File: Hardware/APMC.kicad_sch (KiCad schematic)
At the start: 157 parts, among them J1 Pin header Male 2x7 P:1.27, J10 Conn_01x03, J11 Conn_01x03, J12 Conn_02x08, J13 Conn_01x03, J14 Conn_01x04, J2 USB-C receptacle, J5 Terminal 1x5 P:3.5mm, J6 Terminal 1x5 P:3.5mm, J7 Terminal 1x5 P:3.5mm, J8 Conn_01x04, J9 Conn_01x04, M1 Logo_Open_Hardware_Small, Q1 DMP6023LE, Q2 DMP6023LE, Q3 DMP6023LE, Q4 BSS123, Q5 DMP6023LE, Q6 DMP6023LE, Q7 BSS123, Q8 DMP3056L, U1 LMR51610, U10 TXU0202, U11 PCA9306, U12 LM74703/LM74704, U13 TPS62162DSG, U2 LCFE201202A, U3 TXU0202, U4 M95P32, U5 STM32U575CITx, U6 XTR200, U7 TPS7A2031PDBVR, U8 XTR200, U9 ADS1x2S14, X1 SiT8008Bx-7x, Y1 32.768kHz

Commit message: post-prod fixes
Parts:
- C28: value 1uF/4V -> 4.7uF/4V; footprint Capacitor_SMD:C_0603_1608Metric_Pad1.08x0.95mm_HandSolder -> Custom:C_0603_1608Metric_Pad0.98x0.95mm_HandSolder; Mfg TDK: CGA3E2X5R1A105K080AA -> Samasung: CL10B475KQ8NQNC; Mouser 810-CGA3E2X5R1A105KA -> 187-CL10B475KQ8NQNC; Remarks (none) -> ESR < 20 mΩ @ 3 MHz
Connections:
- net GND: now also C28.1; no longer C28.2
- net VDDA: now also C28.2; no longer C28.1

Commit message: initial firmware
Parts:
- J1: footprint Custom:PinHeader_2x07_P1.27mm_Horizontal -> Custom:PinHeader_2x07_P1.27mm_Horizontal-UP
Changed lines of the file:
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@@
 			)
 		)
-		(property "Footprint" "Custom:PinHeader_2x07_P1.27mm_Horizontal"
+		(property "Footprint" "Custom:PinHeader_2x07_P1.27mm_Horizontal-UP"
 			(at 241.3 26.67 0)
 			(hide yes)

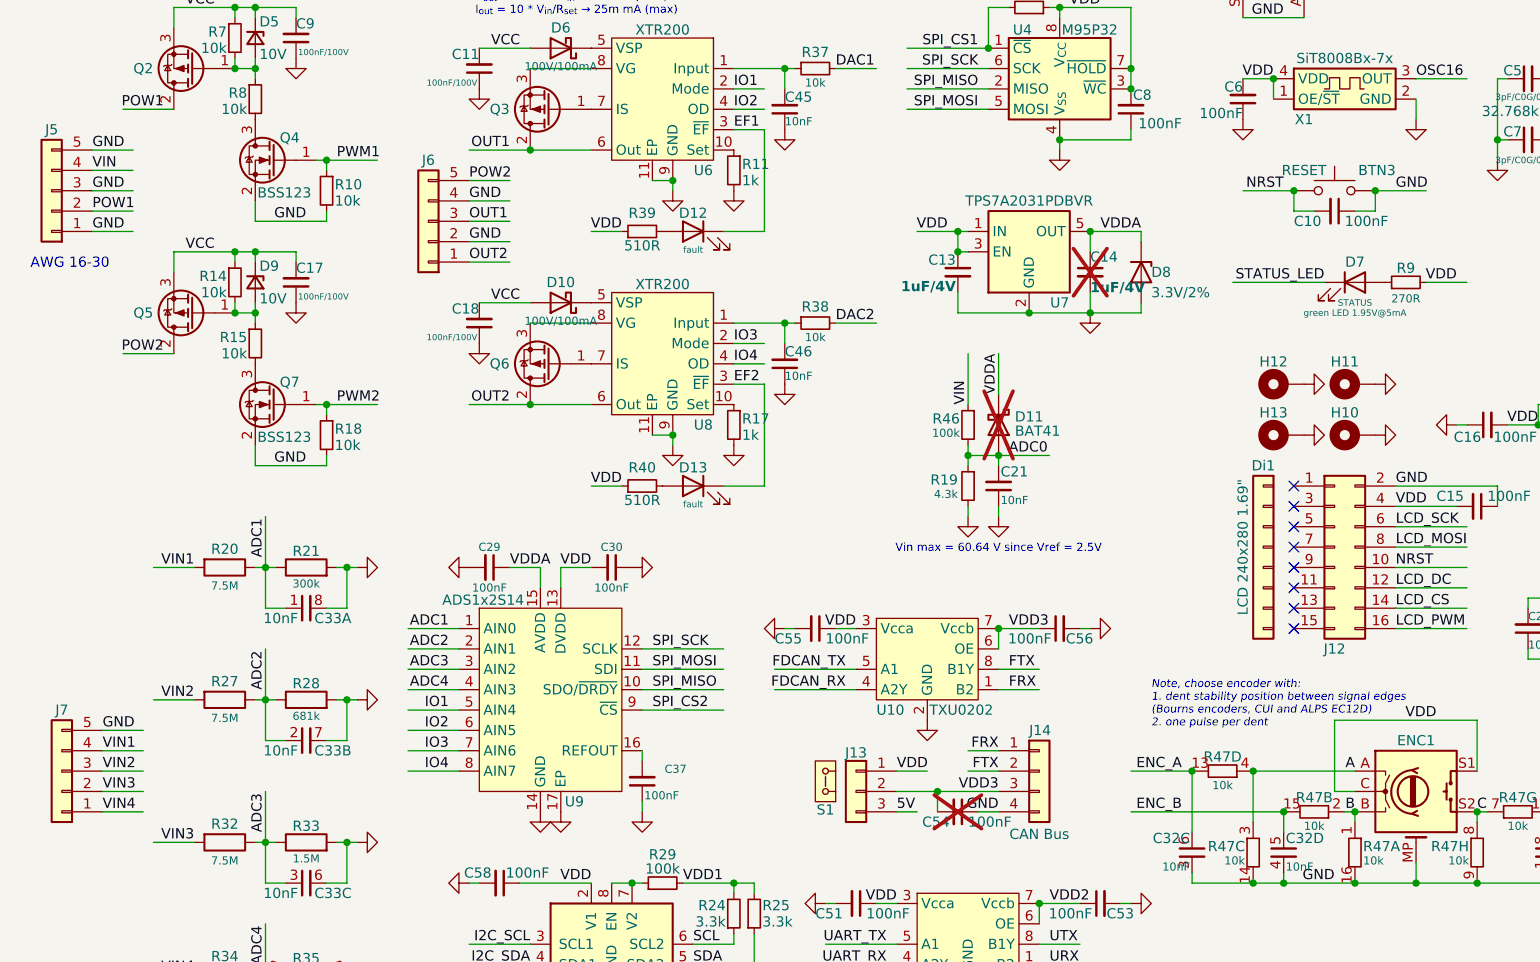
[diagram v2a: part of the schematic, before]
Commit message: LCD pin header modified
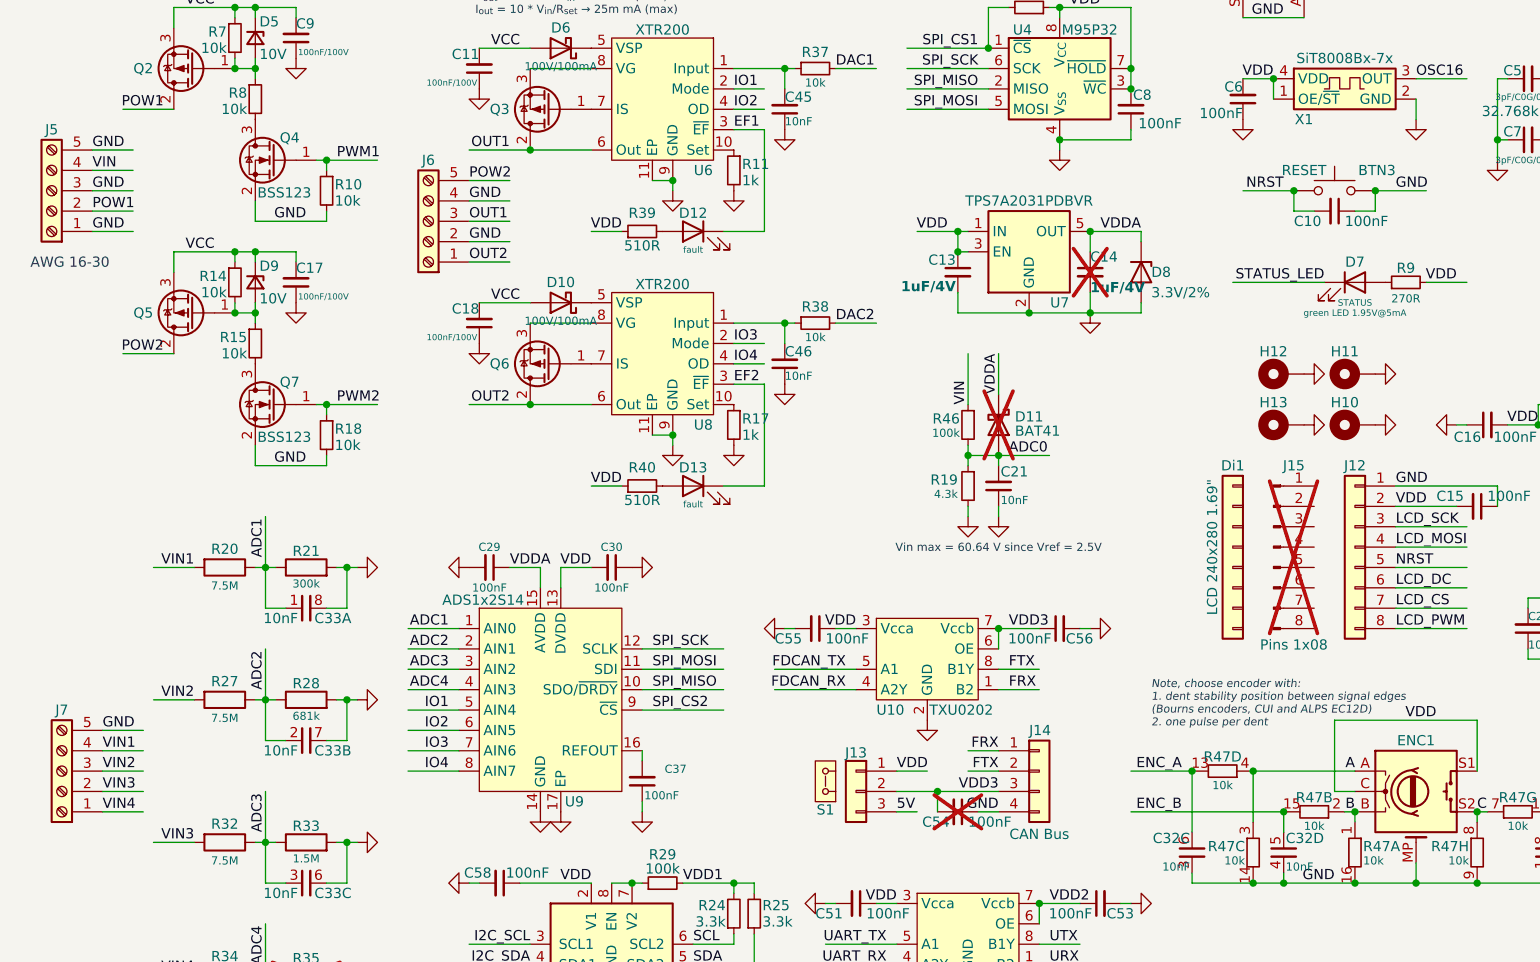
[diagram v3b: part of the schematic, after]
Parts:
- added J15: Pins 1x08, symbol Connector:Conn_01x08_Pin
- J12: value Conn_02x08 -> Conn_01x08; footprint Custom:Harwin_M20-7810845_2x08_P2.54mm_Vertical -> Custom:PinHeader_1x08_P2.54mm_Vertical; symbol Connector_Generic:Conn_02x08_Odd_Even -> Connector_Generic:Conn_01x08; Alt Harwin: M20-7810845, M20-7810845R (2x8, 3.55mm), GCT: BG125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 -> 3M: 929870-01-08-RA, 929984-01-08-RK (H: 3.8mm), Samtec: SL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; Mfg Harwin: M20-7810845 -> 3M: 929870-01-08-30; Mouser 855-M20-7810845 -> 517-929870-01-08-30
- J5, J6, J7: symbol Connector_Generic:Conn_01x05 -> Connector:Screw_Terminal_01x05
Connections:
- net GND: now also J12.1 (Pin_1); no longer J12.2 (Pin_2)
- net LCD_CS: now also J12.7 (Pin_7); no longer J12.14 (Pin_14)
- net LCD_DC: now also J12.6 (Pin_6); no longer J12.12 (Pin_12)
- net LCD_MOSI: now also J12.4 (Pin_4); no longer J12.8 (Pin_8)
- net LCD_PWM: now also J12.8 (Pin_8); no longer J12.16 (Pin_16)
- net LCD_SCK: now also J12.3 (Pin_3); no longer J12.6 (Pin_6)
- net NRST: now also J12.5 (Pin_5); no longer J12.10 (Pin_10)
- net VDD: now also J12.2 (Pin_2); no longer J12.4 (Pin_4)
- no-connect marks 18 -> 10
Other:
- moved on the sheet: Di1, H10, H11, H12, H13

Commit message: rev 2.1 work in progress
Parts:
- removed BTN2: tactile switch 6x6, Custom:tactile_switch_6x6, symbol Switch:SW_Push
- removed C33: 10nF, Custom:RC_Array_Isolated_4_0805, symbol RC_Arrays:C_Array_04_Isolated
- removed Q8: DMP3056L, Package_TO_SOT_SMD:SOT-23, symbol Transistor_FET:VP0610T
- removed R37, R38: 10k, Resistor_SMD:R_0603_1608Metric_Pad0.98x0.95mm_HandSolder, symbol Device:R_Small
- removed R42: 19.1k, Resistor_SMD:R_0603_1608Metric_Pad0.98x0.95mm_HandSolder, symbol Device:R_Small
- removed R43: 100k, Resistor_SMD:R_0603_1608Metric_Pad0.98x0.95mm_HandSolder, symbol Device:R_Small
- removed U1: LMR51610, Package_TO_SOT_SMD:SOT-23-6, symbol LMR51610:LMR51610
- added BTN3: tactile switch 6x6, tactile_switch_6x6_LED, symbol Switch:SW_Push_LED
- added BTN4: SW_Push, Custom:Schurter_MCS-18a, symbol Switch:SW_Push
- added C1, C38, C43: 1uF/10V, Custom:C_0603_1608Metric_Pad0.98x0.95mm_HandSolder, symbol Device:C_Small
- added C31, C33: 1.5nF, Custom:C_0603_1608Metric_Pad0.98x0.95mm_HandSolder, symbol Device:C_Small
- added C34: 100nF, Custom:C_0603_1608Metric_Pad0.98x0.95mm_HandSolder, symbol Device:C_Small
- added C52, C57, C59, C60: 100pF, Custom:0603_0805, symbol Device:C_Small
- added CAP1: M2.5x7, symbol Mechanical:MountingHole
- added D15: Red LED, Custom:LED_0603_1608Metric_Pad1.05x0.95mm_HandSolder, symbol Device:LED
- added D16: TVS 5V U, Custom:D_SOD-123F, symbol Device:D_Zener
- added D57: SS10200HE, Custom:D_SOD-123F, symbol Device:D_Schottky
- added R16: 100k, Resistor_SMD:R_0603_1608Metric_Pad0.98x0.95mm_HandSolder, symbol Device:R_Small
- added R219: 330R/200mA, Resistor_SMD:R_0603_1608Metric_Pad0.98x0.95mm_HandSolder, symbol Device:FerriteBead_Small
- added R22: 5.6k, Resistor_SMD:R_0603_1608Metric_Pad0.98x0.95mm_HandSolder, symbol Device:R_Small
- added R23: 680R, Resistor_SMD:R_0603_1608Metric_Pad0.98x0.95mm_HandSolder, symbol Device:R_Small
- added R4: 360k, Resistor_SMD:R_0603_1608Metric_Pad0.98x0.95mm_HandSolder, symbol Device:R_Small
- added R48, R51: 162k, Resistor_SMD:R_0603_1608Metric_Pad0.98x0.95mm_HandSolder, symbol Device:R_Small
- added R49, R50: 115k, Resistor_SMD:R_0603_1608Metric_Pad0.98x0.95mm_HandSolder, symbol Device:R_Small
- added R52: 64.9k, Resistor_SMD:R_0603_1608Metric_Pad0.98x0.95mm_HandSolder, symbol Device:R_Small
- added U14: OPA2387DSG, Custom:WSON-8-1EP_2x2mm_P0.5mm_EP0.9x1.6mm, symbol Amplifier_Operational:OPA2333xxDRB
- added U15: TPS259461A, Custom:VQFN-HR-10-RPW, symbol TPS2597:TPS259461
- added U16: TUSB320, Package_DFN_QFN:Texas_X2QFN-12_1.6x1.6mm_P0.4mm, symbol TUSB320:TUSB320
- added U17: LMR38015, Custom:TI_WSON-12-1EP_3x3mm_P0.5mm_EP1.3x2.5mm_ThermalVias, symbol LMR380xx:LMR380xx
- BTN2: renamed from BTN1; Alt PTS125SK12-2 LFS, 95C12B4T, 430162085826, TL1100F160Q4JBLK,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 -> TS26-68-25-G-260-SMT-TR; Alt2 (none) -> PTS125SK12-2 LFS, 95C12B4T, 430162085826, TL1100F160Q4JBLK,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; now left out of the parts list
- C13: value 1uF/4V -> 4.7uF/6.3; footprint Capacitor_SMD:C_0603_1608Metric_Pad1.08x0.95mm_HandSolder -> Custom:C_0603_1608Metric_Pad0.98x0.95mm_HandSolder; Mfg TDK: CGA3E2X5R1A105K080AA -> Samasung: CL10B475KQ8NQNC; Mouser 810-CGA3E2X5R1A105KA -> 187-CL10B475KQ8NQNC; Remarks (none) -> ESR < 20 mΩ @ 3 MHz
- C21, C39: Remarks 5%, low-profile (h ≤ 0.5 mm) -> 10%
- C28: value 4.7uF/4V -> 1uF/10V; Mfg Samasung: CL10B475KQ8NQNC -> TDK: CGA3E2X5R1A105M080AA; Mouser 187-CL10B475KQ8NQNC -> 810-CGA3E2X5R1A105MA; Remarks ESR < 20 mΩ @ 3 MHz -> (none)
- C45, C46: value 10nF -> 100pF; Mfg Murata: GRM1857U1A103JA44D -> Samsung: CL10C101JB8NNNC; Mouser 81-GRM1857U1A103JA4D -> 187-CL10C101JB8NNNC; Remarks 5%, low-profile (h ≤ 0.5 mm) -> 5%
- D10: Alt BAT46WJF, BAT46WSHE3-TP, GSBAT46WS, NSR02100HT1G -> BAT46WS, BAT46WJF, BAT46WSHE3-TP, GSBAT46WS, NSR02100HT1G
- Di1: Remarks (none) -> total thickness: 3 mm
- J12: Alt 3M: 929870-01-08-RA, 929984-01-08-RK (H: 3.8mm), Samtec: SL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 -> 3M: 929870-01-08-RA (H: 3.8mm), 929984-01-08-RK (H: 3.8mm),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; Alt2 expensive spring-loaded connector Mill-Max: 821-22-008-10-002101 -> expensive spring-loaded connector Mill-Max: 821-22-008-10-002101 (H: 3.6 mm)
- J15: Remarks Pins to be used with Samtec SL-108-xx and SX-108-xx round p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 -> Pins to be used with Samtec SL-108-x-E (H: 1.78 mm), SL-108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
- J2: value USB-C receptacle -> USB4105-GF-A; symbol Connector:USB_C_Receptacle_USB2.0_16P -> USB_C_Receptacle:USB_C_Receptacle_USB2.0_14P
- L1: value 33uH -> 22uH
- Q1: value DMP6023LE -> FDT86102LZ; Alt TSMC: TSM950N10CW RPG -> (none)
- Q2, Q3, Q5, Q6: Alt MCC: MCT090P10L-TP -> Toshiba: SSM3K7002CFU,LF, NXP: NX138BKWX, DiodesInc: DMN62D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
- R1: value 5.1k -> 11R; Mfg Susumu: RR0816P-512-D -> Susumu: RR0816Q-110-D; Mouser 754-RR0816P-512D -> 754-RR0816Q-110D
- R11, R17: value 1k -> 1.69k; Mfg Susumu: RG1608P-102-B-T5 -> Yageo: RT0603BRD071K69L; Mouser 754-RG1608P-102-B-T5 -> 603-RT0603BRD071K69L
- R2: value 5.1k -> 887k; Mfg Susumu: RR0816P-512-D -> Yageo: RT0603BRD07887KL; Mouser 754-RR0816P-512D -> 603-RT0603BRD07887KL; Remarks 1% -> 1%, resistance must be between 855k - 920k
- R20, R21, R27, R28, R32, R33, R34, R35: footprint Resistor_SMD:R_0805_2012Metric -> Custom:0603_0805
- R29, R44, R6: Mfg Susumu: RG1608P-104-D-T5 -> Susumu: RG1608P-104-B-T5; Mouser 754-RG1608P-104DT5 -> 754-RG1608P-104-B-T5
- R45: value 25.5k -> 27k; Mfg Susumu: RR0816P-2552-D-40C -> Susumu: RR0816P-273-D; Mouser 754-RR0816P-2552D40C -> 754-RR0816P-273D; Remarks 0.5%, use 21k for 6V lower range (Susumu: RG1608P-2102-D-T5) -> 0.5%
- R46: Mfg Susumu: RG1608P-104-D-T5 -> Susumu: RG1608P-104-B-T5; Mouser 754-RG1608P-104DT5 -> 754-RG1608P-104-B-T5; Remarks 0.5%, 25 ppm/°C, 100V min -> 0.1%, 25 ppm/°C, 100V min
- R47: Mouser 603-RT0603DRD0710KL -> 667-EXB-2HV103JV
- R5: value 10k -> 100k; Mfg Yageo: RT0603DRD0710KL -> Susumu: RG1608P-104-B-T5; Mouser 603-RT0603DRD0710KL -> 754-RG1608P-104-B-T5; Notes (none) -> 1%; Remarks 1% -> (none)
- renumbered BTN3 to BTN1
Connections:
- net 5V: now also C43.2, D57.1 (K), R16.1, R219.2, R4.1, U15.5 (IN)
- net ADC1: now also C52.2
- net ADC2: now also C57.2
- net ADC3: now also C59.2
- net ADC4: now also C60.2
- net B: no longer ENC2.B
- net CC1: now also U16.1 (CC1); no longer R1.2
- net CC2: now also U16.2 (CC2); no longer R2.2
- net D: now also BTN3.1, BTN4.2
- net DAC1: now also U14.5 (+)
- net DAC2: now also U14.3 (+)
- net GND: now also C13.1, C1.1, C31.1, C33.1, C34.1, C38.1, C43.1, C52.1, C57.1, C59.1, C60.1, D16.2 (A), R22.1, R48.2, R51.2, R52.2, U14.4 (V-), U14.9 (PAD), U15.8 (GND), U16.10 (GND), U16.11 (~{EN}), U17.1 (GND), U17.13 (GND), U17.2 (GND); no longer C13.2, C45.1, C46.1, R1.1, R2.1
- net I2C_SCL: now also U16.8 (SCL)
- net I2C_SDA: now also U16.7 (SDA)
- net SW: now also U17.11 (SW), U17.12 (SW)
- net USB_VBUS: now also R1.2, R2.1, C1.2, D16.1 (K), U15.6 (OUT)
- net VDD: now also C13.2, BTN3.2, BTN3.4 (A), BTN4.1, C34.2, D15.2 (A), U16.12 (VDD), U16.5 (ADDR); no longer C13.1
- net at C48.1, FB1.1, R44.1: now also U17.5 (VIN), U17.6 (VIN)
- net at C39.2, R44.2, R45.1: now also U17.3 (EN)
- net at C46.2: now also U6.1 (Input), R50.1, U14.7; no longer U8.1 (Input)
- net at C45.2: now also U8.1 (Input), R49.1, U14.1; no longer U6.1 (Input)
- net at C20.2: now also U17.10 (CB)
- net at C3.2, C4.1, FB2.2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: now also U17.8 (FB)
- net at BTN2.3 (K), R36.1: now also BTN3.3 (K)
- new net: C46.1, R50.2, R51.1, U14.6 (-)
- new net: C45.1, R48.1, R49.2, U14.2 (-)
- new net: D15.1 (K), R23.2
- new net: R4.2, U15.1 (EN/UVLO)
- new net: C38.2, R219.1, U14.8 (V+)
- new net: D57.2 (A), R1.1
- new net: R52.1, U17.7 (RT/SYNC)
- new net: R23.1, U15.4 (~{FLT})
- new net: R2.2, U16.4 (VBUS_DET)
- new net: R22.2, U15.9 (ILM)
- new net: C31.2, U15.10 (ITIMER)
- new net: C33.2, U15.7 (DVDT)
- new net PG5: R16.2, U15.2 (OVLO), U16.9 (ID), U17.9 (PG)
- new net USB_INT: U16.6 (~{INT})
- no-connect marks 10 -> 9
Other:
- note added: "6-60 V"
- note added: ">> For Schurter MCS-18a switche use Mill-Max 0300-2-15-01-47-01-10-0 (0.635 - 0.94 mm) 0300-1 L:2.8 mm 0300-2 L:4.75 mm 8300-0 L:3.55 mm or similar single pin female receptacle >> For SameSky (CUI) TS27 switch use TS27-CAP (e.g. TS27-68-24-G-260-D) what to use for TS26? (e.g. TS26-68-25-G-260-SMT-TR)"
- note added: "EN: 1.25/1.1V (5nA)"
- note added: "V_{out} = 3.75V * V_{in} → 9.375 V (max) I_{out} = 10 * V_{in}/R_{set} → 25m mA (max) Output voltage headroom = 2.3 V (max) Maximum output voltage = 18.75 V (V_{IN} = 5V)"
- note added: "address: 0x61 -> 0x47/0x67"
- note removed: "EN: 1.227/1.0V (10nA)"
- note removed: "FB: 0.8V"
- note removed: "V_{out} = 3.75V * V_{in} → 9.375V (max) I_{out} = 10 * V_{in}/R_{set} → 25m mA (max)"
- moved on the sheet: BT1, BTN1, BTN2, C10, C11, C12, C14, C15, C17, C18, C20, C21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

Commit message: refinement
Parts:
- H1: value M2.5x7 -> M2.5x6; Alt Harwin: R25-1000702, Wurth: 970070151, 970070154, 970070155 -> M2.5x6 >> Harwin: R25-1000602; Alt2 (none) -> M2.5x7 >> Harwin: R25-1000702, Wurth: 970070151, 970070154,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; Mfg Harwin: R25-1000702 -> Harwin: R25-1000602; Mouser 855-R25-1000702 -> 855-R25-1000602
- H10, H11, H12: value Standoff_M2x4.0 -> Standoff_M2x3.0; Alt (none) -> L: 4.0 mm >> Wurth: 9774040243R; Mfg Wurth: 9774040243R -> Wurth: 9774030243R; Mouser 710-9774040243R -> 710-9774030243R; Remarks D ≤ 4.35, L = 4.0 mm -> (none)
- H13: value Standoff_M2x4.0 -> Standoff_M2x3.0; Alt (none) -> L: 4.0 mm >> Wurth: 9774040243R; Mouser 710-9774040243R -> 710-9774030243R; Remarks D ≤ 4.35, L = 4.0 mm -> (none)
- H2, H3, H4: value M2.5x7 -> M2.5x6; Mfg Harwin: R25-1000702 -> Harwin: R25-1000602; Mouser 855-R25-1000702 -> 855-R25-1000602
- L2: Remarks (none) -> height 2.8 mm (max)

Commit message: Schematic update
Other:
- note removed: ">> For Schurter MCS-18a switche use Mill-Max 0300-2-15-01-47-01-10-0 (0.635 - 0.94 mm) 0300-1 L:2.8 mm 0300-2 L:4.75 mm 8300-0 L:3.55 mm or similar single pin female receptacle >> For SameSky (CUI) TS27 switch use TS27-CAP (e.g. TS27-68-24-G-260-D) what to use for TS26? (e.g. TS26-68-25-G-260-SMT-TR)"
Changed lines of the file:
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@@
-		)
-	)
-	(text ">> For Schurter MCS-18a switche use\nMill-Max 0300-2-15-01-47-01-10-0 (0.635 - 0.94 mm)\n0300-1 L:2.8 mm\n0300-2 L:4.75 mm\n8300-0 L:3.55 mm\nor similar single pin female receptacle\n>> For SameSky (CUI) TS27 switch use TS27-CAP\n(e.g. TS27-68-24-G-260-D)\nwhat to use for TS26? (e.g. TS26-68-25-G-260-SMT-TR)"
-		(exclude_from_sim no)
-		(at 215.138 172.212 0)
-		(effects
-			(font
-				(size 1.016 1.016)
-				(thickness 0.127)
-				(color 0 0 194 1)
-			)
-			(justify left top)
 		)
 	)

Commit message: BOM fix
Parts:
- H13: Mfg Wurth: 9774040243R -> Wurth: 9774030243R
- U5: Alt STM32U575CIT6, STM32U585CIT6 (2MB flash, 786k SRAM) -> 2MB flash, 786k SRAM, DMA2D >> STM32U575CIT6, STM32U585CIT6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; Alt2 STM32U535CET6, STM32U545CET6 (no DMA2D, 512k flash, 274k SR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 -> 512k flash, 274k SRAM, no DMA2D >> STM32U535CET6, STM32U545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

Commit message: refinement
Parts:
- CAP1: value M2.5x7 -> button cap
- J1: footprint Custom:PinHeader_2x07_P1.27mm_Horizontal-UP -> Custom:PinHeader_2x07_P1.27mm_Horizontal-UP-0.15
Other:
- moved on the sheet: C38, C43, R219, U14C
